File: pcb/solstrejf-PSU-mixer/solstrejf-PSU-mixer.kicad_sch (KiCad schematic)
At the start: 7 parts, among them J1 LEFT_JACK, J2 RIGHT_JACK, J3 Conn_02x05_Odd_Even, J4 Conn_02x05_Odd_Even, J5 Conn_02x05_Odd_Even, J6 Conn_02x05_Odd_Even, J7 Transformer_Terminals

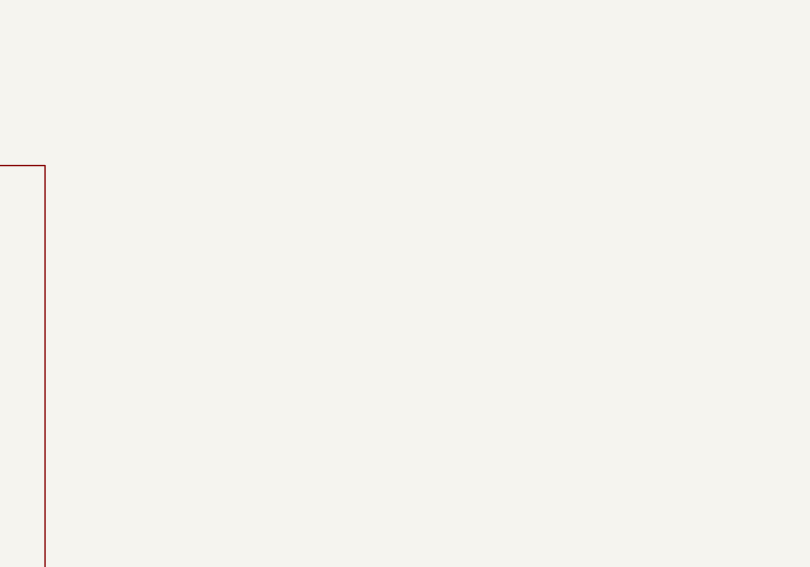
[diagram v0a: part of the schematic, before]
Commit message: made first attempt of a PCB layout onf the PSU/mixer. No routing performed. Minor updates to schematic, including mounting holes.
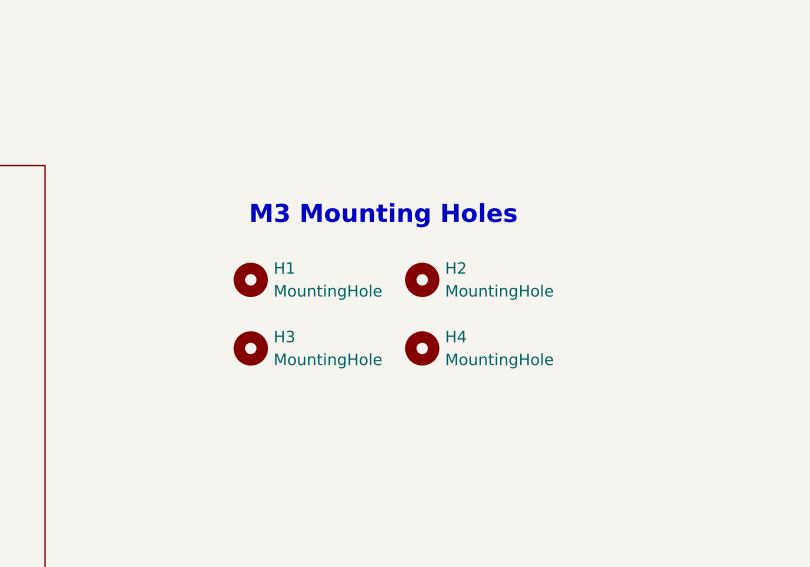
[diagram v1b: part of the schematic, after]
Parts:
- added H1, H2, H3, H4: MountingHole, MountingHole:MountingHole_3.2mm_M3_DIN965, symbol Mechanical:MountingHole
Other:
- note added: "M3 Mounting Holes"

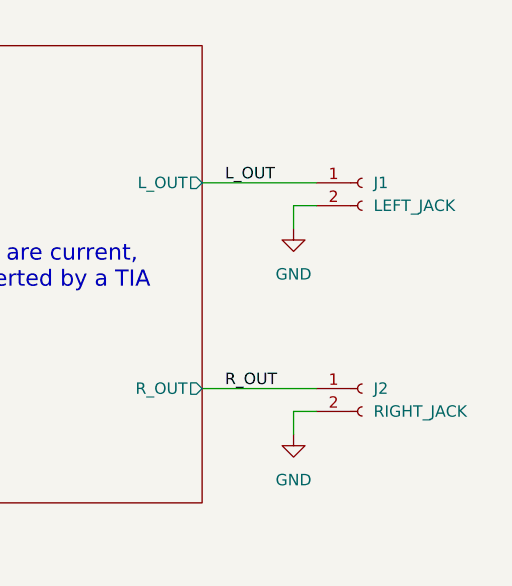
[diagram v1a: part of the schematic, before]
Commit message: routing of PSU/mixer done! Minor schematic updates. Added gerber production files to .gitignore.
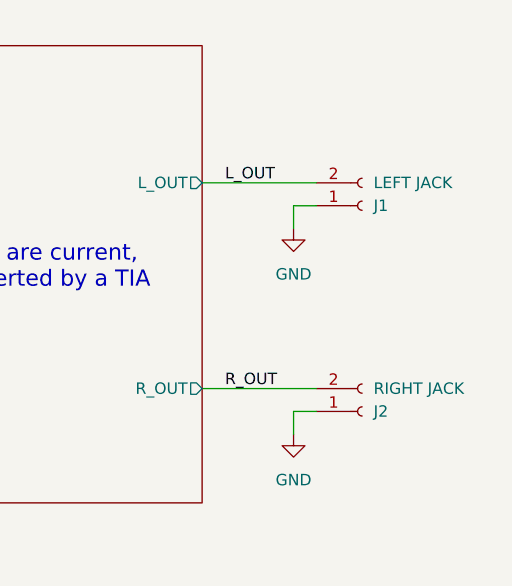
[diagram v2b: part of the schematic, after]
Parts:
- J1: value LEFT_JACK -> LEFT JACK
- J2: value RIGHT_JACK -> RIGHT JACK
- J7: footprint TerminalBlock:TerminalBlock_bornier-3_P5.08mm -> Connector_Wire:SolderWire-0.5sqmm_1x03_P4.8mm_D0.9mm_OD2.3mm
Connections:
- net GND: now also J1.1 (Pin_1), J2.1 (Pin_1); no longer J1.2 (Pin_2), J2.2 (Pin_2)
- net L_OUT: now also J1.2 (Pin_2); no longer J1.1 (Pin_1)
- net R_OUT: now also J2.2 (Pin_2); no longer J2.1 (Pin_1)
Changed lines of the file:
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@@
 	(symbol
 		(lib_id "Connector:Conn_01x02_Socket")
-		(at 233.68 88.9 0)
-		(unit 1)
-		(exclude_from_sim no)
-		(in_bom yes)
-		(on_board yes)
-		(dnp no)
-		(fields_autoplaced yes)
+		(at 233.68 91.44 0)
+		(mirror x)
+		(unit 1)
+		(exclude_from_sim no)
+		(in_bom yes)
+		(on_board yes)
+		(dnp no)
 		(property "Reference" "J2"
-			(at 234.95 88.8999 0)
-			(effects
-				(font
-					(size 1.27 1.27)
-				)
-				(justify left)
-			)
-		)
-		(property "Value" "RIGHT_JACK"
-			(at 234.95 91.4399 0)
+			(at 234.95 91.4401 0)
+			(effects
+				(font
+					(size 1.27 1.27)
+				)
+				(justify left)
+			)
+		)
+		(property "Value" "RIGHT JACK"
+			(at 234.95 88.9001 0)
 			(effects
 				(font
@@
 		)
 		(property "Footprint" "Connector_PinHeader_2.54mm:PinHeader_1x02_P2.54mm_Vertical"
-			(at 233.68 88.9 0)
+			(at 233.68 91.44 0)
 			(effects
 				(font
@@
 		)
 		(property "Datasheet" "~"
-			(at 233.68 88.9 0)
+			(at 233.68 91.44 0)
 			(effects
 				(font
@@
 		)
 		(property "Description" "Generic connector, single row, 01x02, script generated"
-			(at 233.68 88.9 0)
+			(at 233.68 91.44 0)
 			(effects
 				(font
@@
 	(symbol
 		(lib_id "Connector:Conn_01x02_Socket")
-		(at 233.68 66.04 0)
-		(unit 1)
-		(exclude_from_sim no)
-		(in_bom yes)
-		(on_board yes)
-		(dnp no)
-		(fields_autoplaced yes)
+		(at 233.68 68.58 0)
+		(mirror x)
+		(unit 1)
+		(exclude_from_sim no)
+		(in_bom yes)
+		(on_board yes)
+		(dnp no)
 		(property "Reference" "J1"
-			(at 234.95 66.0399 0)
-			(effects
-				(font
-					(size 1.27 1.27)
-				)
-				(justify left)
-			)
-		)
-		(property "Value" "LEFT_JACK"
-			(at 234.95 68.5799 0)
+			(at 234.95 68.5801 0)
+			(effects
+				(font
+					(size 1.27 1.27)
+				)
+				(justify left)
+			)
+		)
+		(property "Value" "LEFT JACK"
+			(at 234.95 66.0401 0)
 			(effects
 				(font
@@
 		)
 		(property "Footprint" "Connector_PinHeader_2.54mm:PinHeader_1x02_P2.54mm_Vertical"
-			(at 233.68 66.04 0)
+			(at 233.68 68.58 0)
 			(effects
 				(font
@@
 		)
 		(property "Datasheet" "~"
-			(at 233.68 66.04 0)
+			(at 233.68 68.58 0)
 			(effects
 				(font
@@
 		)
 		(property "Description" "Generic connector, single row, 01x02, script generated"
-			(at 233.68 66.04 0)
+			(at 233.68 68.58 0)
 			(effects
 				(font
@@
 			)
 		)
-		(property "Footprint" "TerminalBlock:TerminalBlock_bornier-3_P5.08mm"
+		(property "Footprint" "Connector_Wire:SolderWire-0.5sqmm_1x03_P4.8mm_D0.9mm_OD2.3mm"
 			(at 44.45 152.4 0)
 			(effects

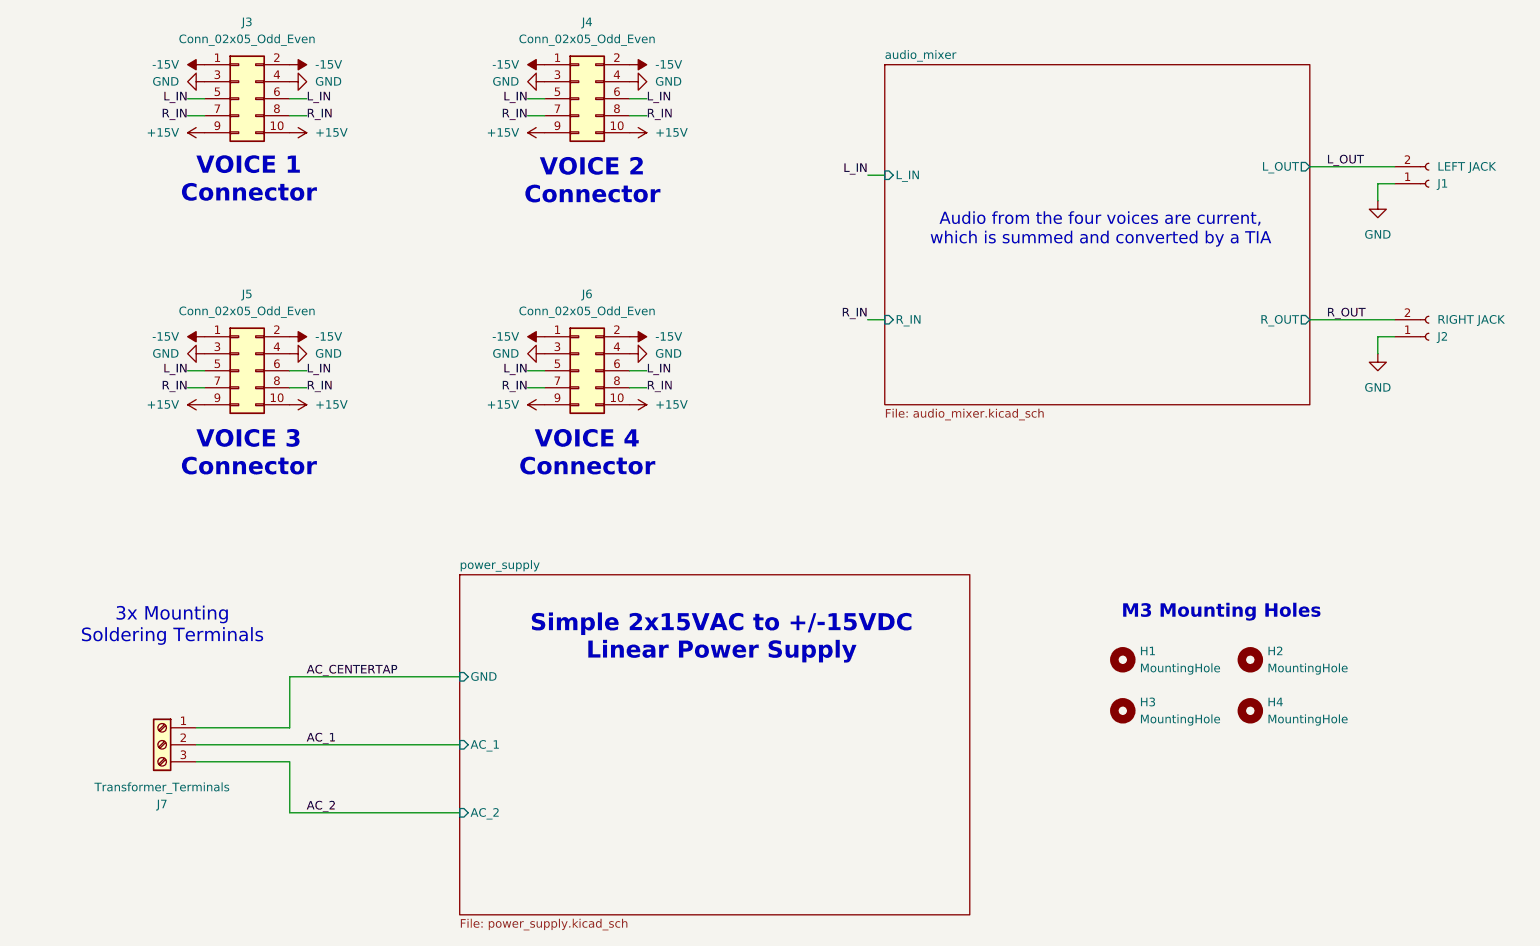
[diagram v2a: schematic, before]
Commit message: Updated fonts in PSU+mixer schematic. Added a print of the PSU+mixer schemtic in new  directory.
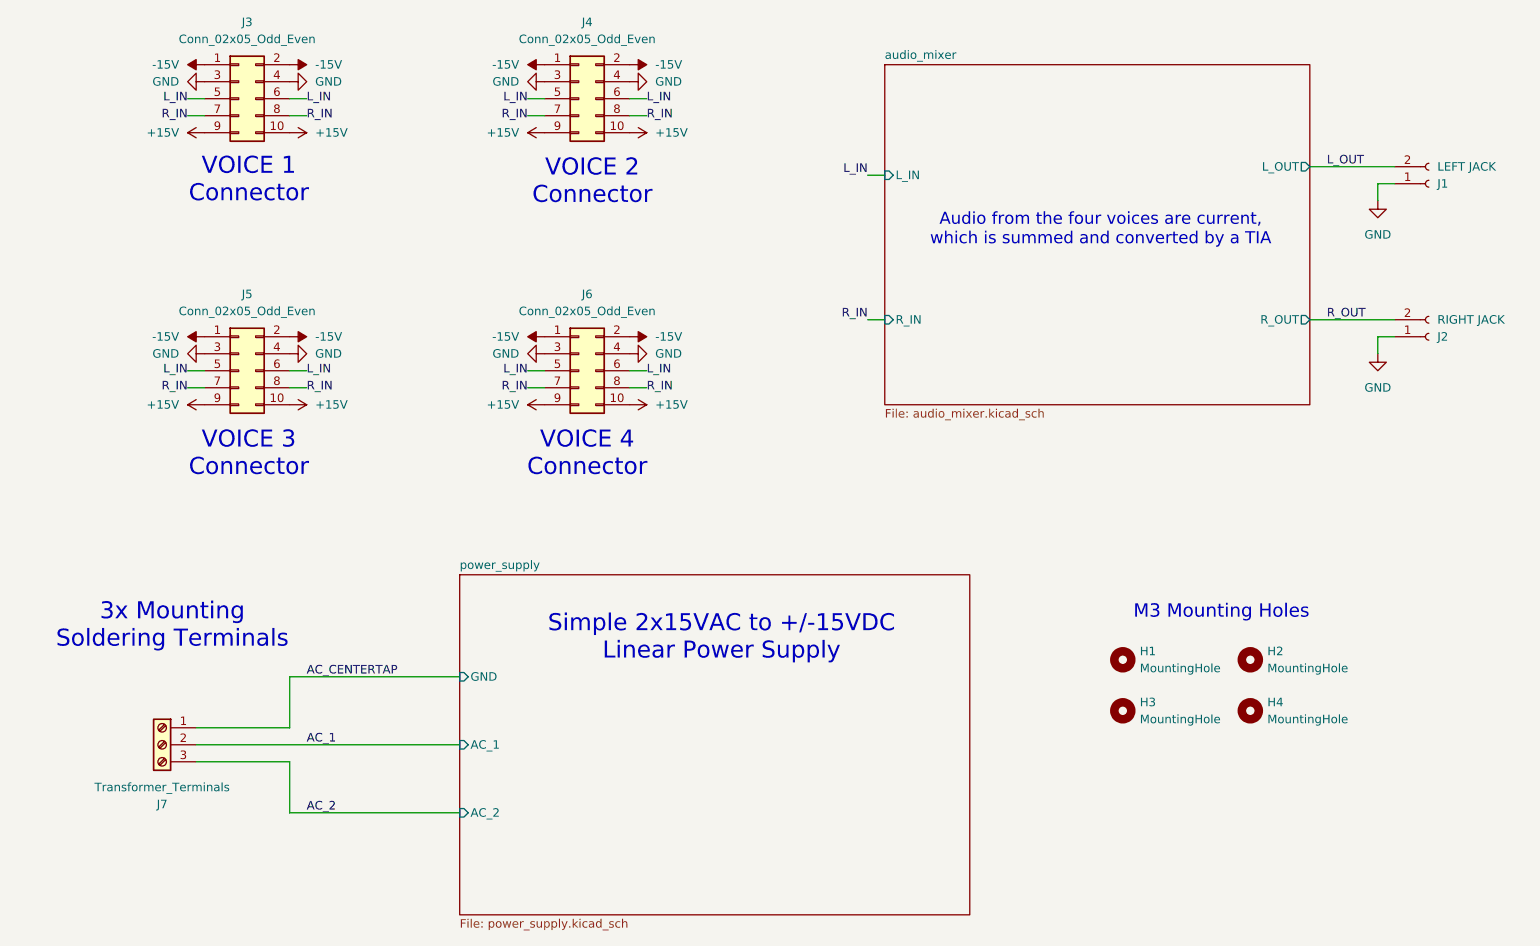
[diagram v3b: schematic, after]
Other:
- title: (none) -> Solstrejf PSU & Mixer
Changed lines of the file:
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@@
 	(generator_version "8.0")
 	(paper "A4")
+	(title_block
+		(title "Solstrejf PSU & Mixer")
+		(date "2024-08-24")
+		(rev "1.0")
+	)
 	(wire
 		(pts
@@
 			(font
 				(size 2.54 2.54)
-				(thickness 0.508)
-				(bold yes)
 			)
 		)
@@
 			(font
 				(size 2 2)
-				(thickness 0.4)
-				(bold yes)
 			)
 		)
@@
 		(effects
 			(font
-				(size 2 2)
+				(size 2.54 2.54)
 			)
 		)
@@
 		(effects
 			(font
-				(size 2.57 2.57)
-				(thickness 0.514)
-				(bold yes)
+				(size 2.54 2.54)
 			)
 		)
@@
 		(effects
 			(font
-				(size 2.57 2.57)
-				(thickness 0.514)
-				(bold yes)
+				(size 2.54 2.54)
 			)
 		)
@@
 		(effects
 			(font
-				(size 2.57 2.57)
-				(thickness 0.514)
-				(bold yes)
+				(size 2.54 2.54)
 			)
 		)
@@
 		(effects
 			(font
-				(size 2.57 2.57)
-				(thickness 0.514)
-				(bold yes)
-			)
-		)
+				(size 2.54 2.54)
+			)
+		)

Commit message: Saved Solstrejf Kicad files in 9.0 format
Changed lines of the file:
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@@
 (kicad_sch
-	(version 20231120)
+	(version 20250114)
 	(generator "eeschema")
-	(generator_version "8.0")
+	(generator_version "9.0")
 	(paper "A4")
 	(title_block
@@
 		(rev "1.0")
 	)
+	(text "Audio from the four voices are current, \nwhich is summed and converted by a TIA"
+		(exclude_from_sim no)
+		(at 184.658 75.438 0)
+		(effects
+			(font
+				(size 1.8 1.8)
+			)
+		)
+	)
+	(text "Simple 2x15VAC to +/-15VDC\nLinear Power Supply"
+		(exclude_from_sim no)
+		(at 128.016 136.398 0)
+		(effects
+			(font
+				(size 2.54 2.54)
+			)
+		)
+	)
+	(text "M3 Mounting Holes"
+		(exclude_from_sim no)
+		(at 202.692 132.588 0)
+		(effects
+			(font
+				(size 2 2)
+			)
+		)
+	)
+	(text "3x Mounting \nSoldering Terminals"
+		(exclude_from_sim no)
+		(at 45.974 134.62 0)
+		(effects
+			(font
+				(size 2.54 2.54)
+			)
+		)
+	)
+	(text "VOICE 2\nConnector"
+		(exclude_from_sim no)
+		(at 108.712 68.326 0)
+		(effects
+			(font
+				(size 2.54 2.54)
+			)
+		)
+	)
+	(text "VOICE 1\nConnector"
+		(exclude_from_sim no)
+		(at 57.404 68.072 0)
+		(effects
+			(font
+				(size 2.54 2.54)
+			)
+		)
+	)
+	(text "VOICE 4\nConnector"
+		(exclude_from_sim no)
+		(at 107.95 108.966 0)
+		(effects
+			(font
+				(size 2.54 2.54)
+			)
+		)
+	)
+	(text "VOICE 3\nConnector"
+		(exclude_from_sim no)
+		(at 57.404 108.966 0)
+		(effects
+			(font
+				(size 2.54 2.54)
+			)
+		)
+	)
 	(wire
 		(pts
@@
 		)
 	)
-	(text "Audio from the four voices are current, \nwhich is summed and converted by a TIA"
-		(exclude_from_sim no)
-		(at 184.658 75.438 0)
-		(effects
-			(font
-				(size 1.8 1.8)
-			)
-		)
-	)
-	(text "Simple 2x15VAC to +/-15VDC\nLinear Power Supply"
-		(exclude_from_sim no)
-		(at 128.016 136.398 0)
-		(effects
-			(font
-				(size 2.54 2.54)
-			)
-		)
-	)
-	(text "M3 Mounting Holes"
-		(exclude_from_sim no)
-		(at 202.692 132.588 0)
-		(effects
-			(font
-				(size 2 2)
-			)
-		)
-	)
-	(text "3x Mounting \nSoldering Terminals"
-		(exclude_from_sim no)
-		(at 45.974 134.62 0)
-		(effects
-			(font
-				(size 2.54 2.54)
-			)
-		)
-	)
-	(text "VOICE 2\nConnector"
-		(exclude_from_sim no)
-		(at 108.712 68.326 0)
-		(effects
-			(font
-				(size 2.54 2.54)
-			)
-		)
-	)
-	(text "VOICE 1\nConnector"
-		(exclude_from_sim no)
-		(at 57.404 68.072 0)
-		(effects
-			(font
-				(size 2.54 2.54)
-			)
-		)
-	)
-	(text "VOICE 4\nConnector"
-		(exclude_from_sim no)
-		(at 107.95 108.966 0)
-		(effects
-			(font
-				(size 2.54 2.54)
-			)
-		)
-	)
-	(text "VOICE 3\nConnector"
-		(exclude_from_sim no)
-		(at 57.404 108.966 0)
-		(effects
-			(font
-				(size 2.54 2.54)
-			)
-		)
-	)
 	(label "L_IN"
 		(at 48.26 55.88 180)
-		(fields_autoplaced yes)
 		(effects
 			(font
@@
 	(label "L_IN"
 		(at 48.26 96.52 180)
-		(fields_autoplaced yes)
 		(effects
 			(font
@@
 	(label "R_IN"
 		(at 99.06 99.06 180)
-		(fields_autoplaced yes)
 		(effects
 			(font
@@
 	(label "L_IN"
 		(at 116.84 96.52 0)
-		(fields_autoplaced yes)
 		(effects
 			(font
@@
 	(label "R_IN"
 		(at 48.26 99.06 180)
-		(fields_autoplaced yes)
 		(effects
 			(font
@@
 	(label "L_IN"
 		(at 99.06 96.52 180)
-		(fields_autoplaced yes)
 		(effects
 			(font
@@
 	(label "R_IN"
 		(at 66.04 99.06 0)
-		(fields_autoplaced yes)
 		(effects
 			(font
@@
 	(label "L_OUT"
 		(at 218.44 66.04 0)
-		(fields_autoplaced yes)
 		(effects
 			(font
@@
 	(label "R_IN"
 		(at 66.04 58.42 0)
-		(fields_autoplaced yes)
 		(effects
 			(font
@@
 	(label "L_IN"
 		(at 149.86 67.31 180)
-		(fields_autoplaced yes)
 		(effects
 			(font
@@
 	(label "AC_2"
 		(at 66.04 162.56 0)
-		(fields_autoplaced yes)
 		(effects
 			(font
@@
 	(label "AC_CENTERTAP"
 		(at 66.04 142.24 0)
-		(fields_autoplaced yes)
 		(effects
 			(font
@@
 	(label "R_IN"
 		(at 149.86 88.9 180)
-		(fields_autoplaced yes)
 		(effects
 			(font
@@
 	(label "R_IN"
 		(at 99.06 58.42 180)
-		(fields_autoplaced yes)
 		(effects
 			(font
@@
 	(label "L_IN"
 		(at 66.04 96.52 0)
-		(fields_autoplaced yes)
 		(effects
 			(font
@@
 	(label "L_IN"
 		(at 99.06 55.88 180)
-		(fields_autoplaced yes)
 		(effects
 			(font
@@
 	(label "L_IN"
 		(at 116.84 55.88 0)
-		(fields_autoplaced yes)
 		(effects
 			(font
@@
 	(label "AC_1"
 		(at 66.04 152.4 0)
-		(fields_autoplaced yes)
 		(effects
 			(font
@@
 	(label "R_IN"
 		(at 48.26 58.42 180)
-		(fields_autoplaced yes)
 		(effects
 			(font
@@
 	(label "R_IN"
 		(at 116.84 99.06 0)
-		(fields_autoplaced yes)
 		(effects
 			(font
@@
 	(label "L_IN"
 		(at 66.04 55.88 0)
-		(fields_autoplaced yes)
 		(effects
 			(font
@@
 	(label "R_IN"
 		(at 116.84 58.42 0)
-		(fields_autoplaced yes)
 		(effects
 			(font
@@
 	(label "R_OUT"
 		(at 218.44 88.9 0)
-		(fields_autoplaced yes)
 		(effects
 			(font
@@
 		(at 152.4 50.8)
 		(size 63.5 50.8)
+		(exclude_from_sim no)
+		(in_bom yes)
+		(on_board yes)
+		(dnp no)
 		(fields_autoplaced yes)
 		(stroke
@@
 		(at 88.9 127)
 		(size 76.2 50.8)
+		(exclude_from_sim no)
+		(in_bom yes)
+		(on_board yes)
+		(dnp no)
 		(fields_autoplaced yes)
 		(stroke
@@
 		)
 	)
+	(embedded_fonts no)
 )
